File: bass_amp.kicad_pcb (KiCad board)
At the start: 2 copper layers, 70.9 x 25.9 mm, 21 parts, among them J1 AudioJack3, J2 PICKUP_SIGNAL, J3 PICKUP_GND, J4 BAT+, J5 BAT-, Q1 BC547, Q2 BC547, SW1 SW_Push_DPDT

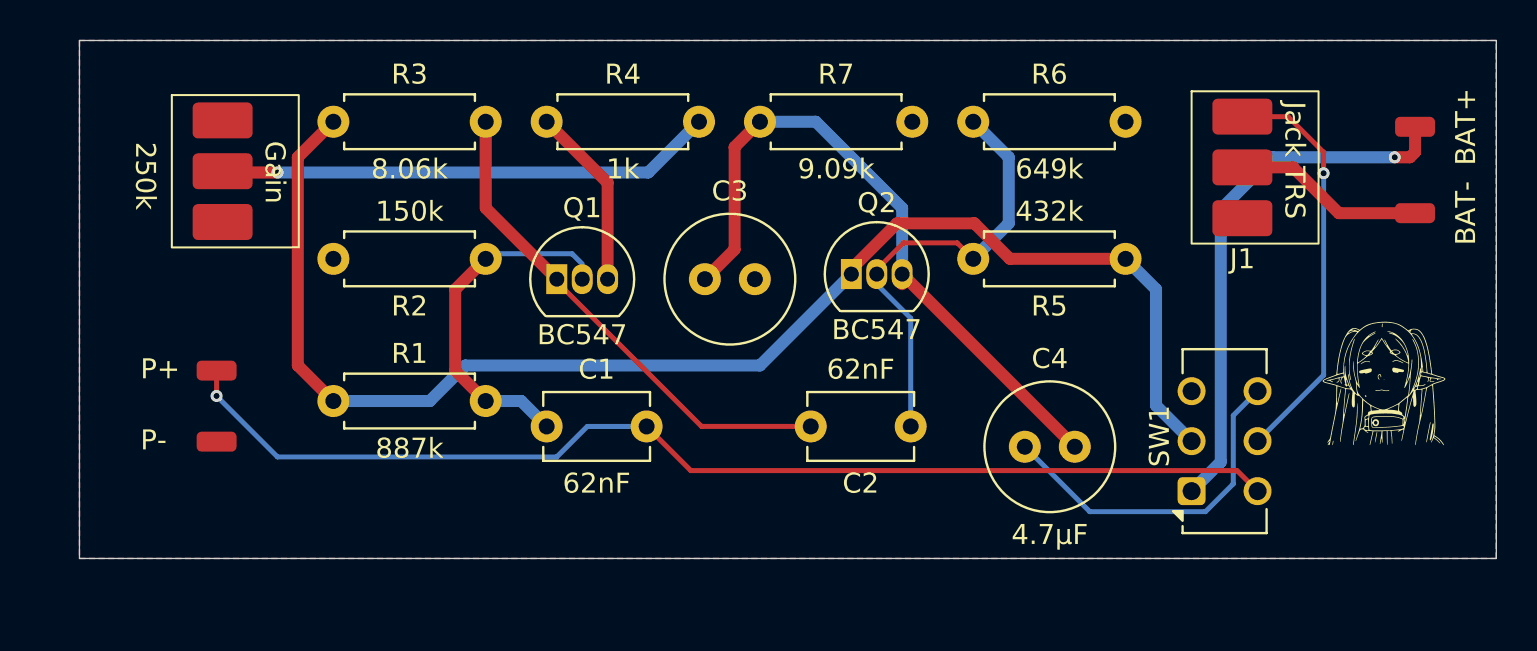
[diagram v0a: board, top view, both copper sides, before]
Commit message: Add mounting holes and update the logo
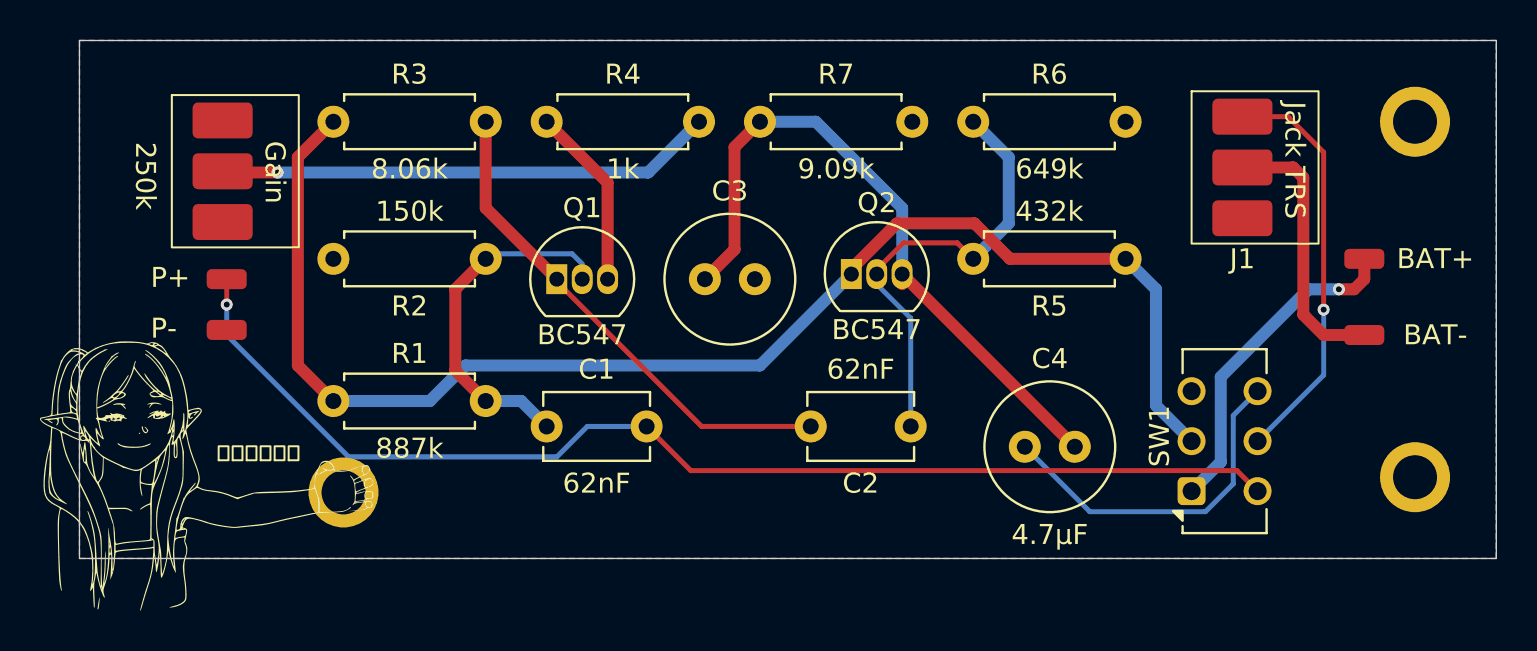
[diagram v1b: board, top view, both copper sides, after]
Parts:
- added REF**: MountingHole_2.2mm_M2_ISO7380_Pad, MountingHole:MountingHole_2.2mm_M2_ISO7380_Pad, F.Cu at (130.0, 83.6)
- added REF**: MountingHole_2.2mm_M2_ISO7380_Pad, MountingHole:MountingHole_2.2mm_M2_ISO7380_Pad, F.Cu at (183.6, 82.8)
- added REF**: MountingHole_2.2mm_M2_ISO7380_Pad, MountingHole:MountingHole_2.2mm_M2_ISO7380_Pad, F.Cu at (183.6, 65.0)
- moved G*** 59.1 mm to (123.2, 82.8)
- moved J4 7.08 mm to (181.1, 71.9)
- moved J5 6.60 mm to (181.1, 75.7)
- moved J3 5.61 mm to (124.2, 75.4)
- moved J2 4.60 mm to (124.2, 72.9)
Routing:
- net +9V: track 26.9 -> 16.5 mm
- net -BATT: track 9.58 -> 13.6 mm
- net SIGNAL_IN: track 56.6 -> 58.9 mm
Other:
- board text added: "いただきます"
